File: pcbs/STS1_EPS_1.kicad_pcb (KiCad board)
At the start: 4 copper layers, 81 x 85 mm, 159 parts, among them J1 Inter-EPS, J2 Panel Y+, J4 Panel Y-, J5 Panel X+, J6 Panel X-, J7 Panel Z-, Q1 SI7135DP-T1-GE3, Q2 SI7135DP-T1-GE3, Q3 SI7135DP-T1-GE3, Q4 2N7002, Q5 2N7002, Q6 2N7002, Q7 2N7002, U1 LTC4020EUHFPBF, U10 MAX11632EEGT, U11 INA180A4, U12 BD50GA5WEFJ, U13 TPS259472ARPW, U14 LM334M, U15 LM334M, U16 LM334M, U17 LM334M, U18 LM334M, U19 TPS259472ARPW, U2 SI7272DP-T1-GE3, U20 TPS259472ARPW, U21 TPS259472ARPW, U22 TPS259472ARPW, U23 TPS259472ARPW, U24 TPS259472ARPW, U27 LTC4451AV#TRMPBF, U28 LTC4451AV#TRMPBF, U3 SI7272DP-T1-GE3, U4 TPS259472ARPW, U5 MAX11632EEGT, U6 MAX11632EEGT, U7 MAX11632EEGT, U8 MAX11632EEGT, U9 MAX11632EEGT

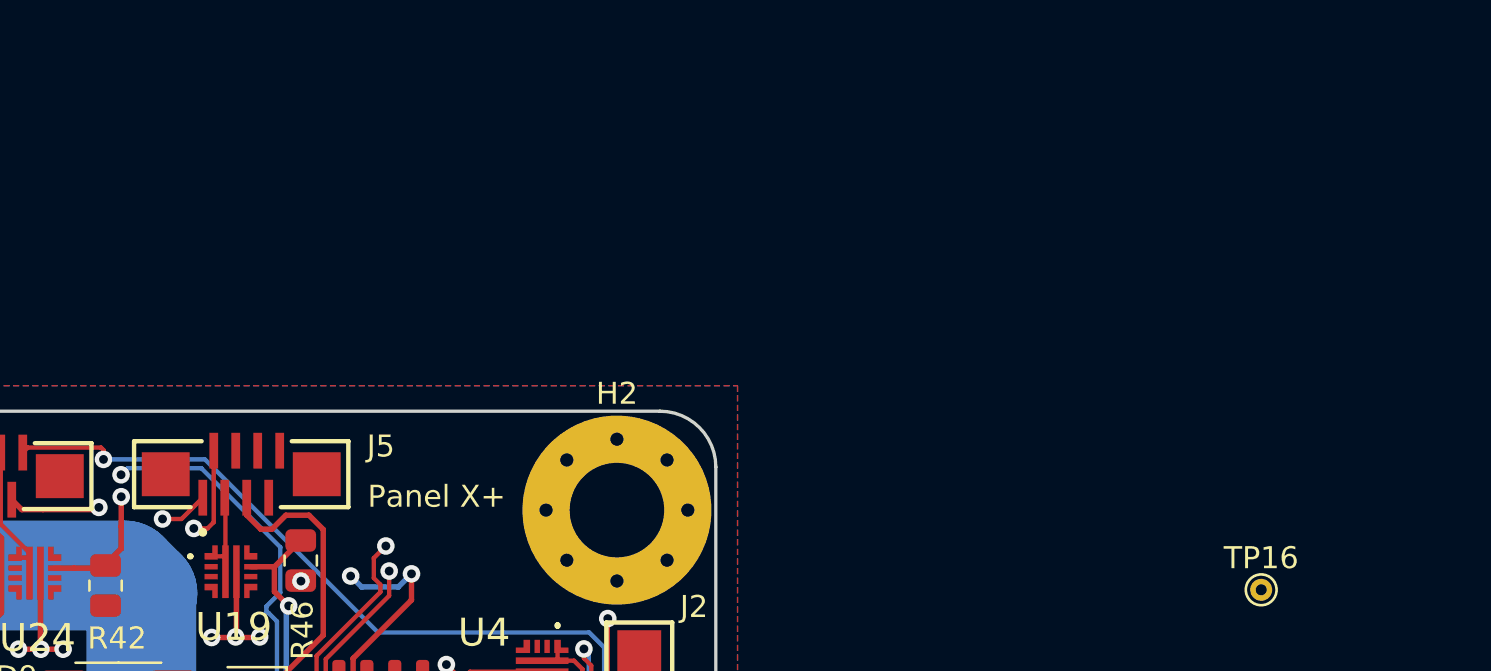
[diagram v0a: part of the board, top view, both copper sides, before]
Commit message: Removed UCI connector from STS1_EPS_2 and merged UCI connector with J5 on STS1_EPS_1.
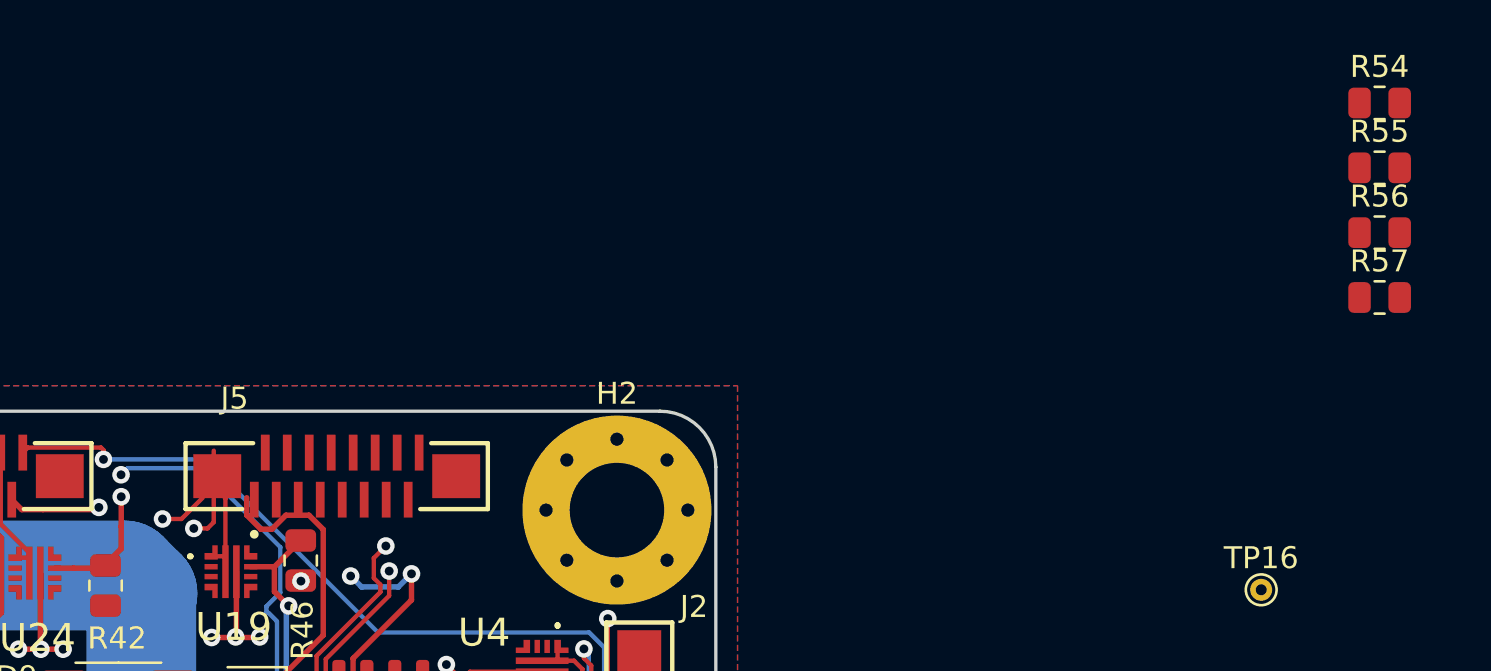
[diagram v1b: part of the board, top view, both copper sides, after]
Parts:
- added R54: 820, Resistor_SMD:R_0805_2012Metric, F.Cu at (176.9, 67.3)
- added R55: 332k, Resistor_SMD:R_0805_2012Metric, F.Cu at (176.9, 70.3)
- added R56: 332k, Resistor_SMD:R_0805_2012Metric, F.Cu at (176.9, 73.2)
- added R57: 390k, Resistor_SMD:R_0805_2012Metric, F.Cu at (176.9, 76.2)
- J5: footprint STS_Connector:SAMTEC_ZF5S-08-03-T-WT -> STS_Connector:SAMTEC_ZF5S-16-03-T-WT
- moved J5 4.34 mm to (129.4, 84.3)
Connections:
- net /Cubesat Bus Interface/UCI_COBC_UART_1 renamed /Cubesat Bus Interface/UCI_COBC_UART_TX
- net /Cubesat Bus Interface/UCI_COBC_UART_2 renamed /Cubesat Bus Interface/UCI_COBC_UART_RX
- CSBI_2 pad 13: /BAT_FAULT -> Net-(CSBI_2-Pin_13)
- CSBI_2 pad 14: /BAT_FAULT -> Net-(CSBI_2-Pin_13)
- CSBI_2 pad 17: GND -> Net-(CSBI_2-Pin_17)
- CSBI_2 pad 18: GND -> Net-(CSBI_2-Pin_17)
- CSBI_2 pad 19: Net-(CSBI_2-Pin_19) -> /BAT_FAULT
- CSBI_2 pad 20: Net-(CSBI_2-Pin_19) -> /BAT_FAULT
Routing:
- net Net-(CSBI_2-Pin_19): track 2.00 -> 0.00 mm
- net Net-(CSBI_2-Pin_17): track 0.00 -> 2.00 mm
- net GND: track 106.2 -> 104.2 mm
- net /BAT_FAULT: track 75.1 -> 77.1 mm

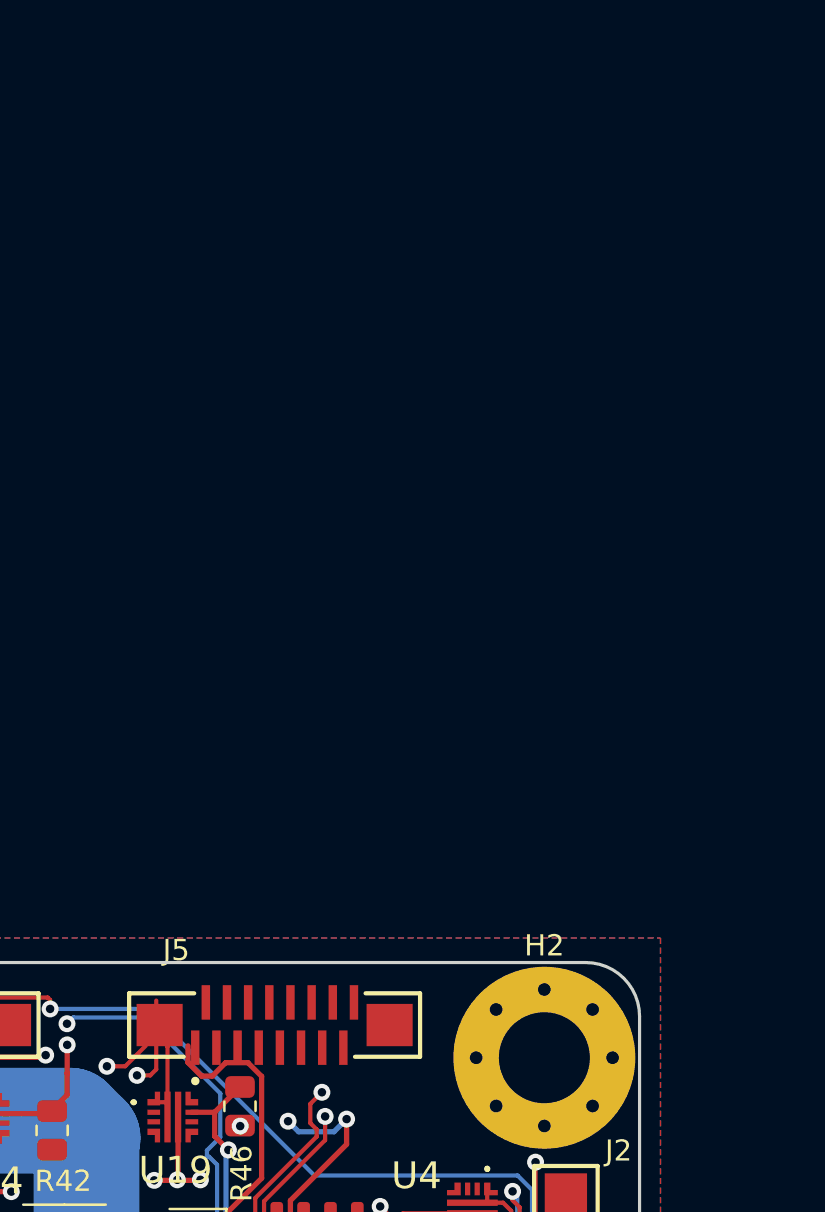
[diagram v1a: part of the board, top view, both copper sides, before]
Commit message: Added TVS diodes.
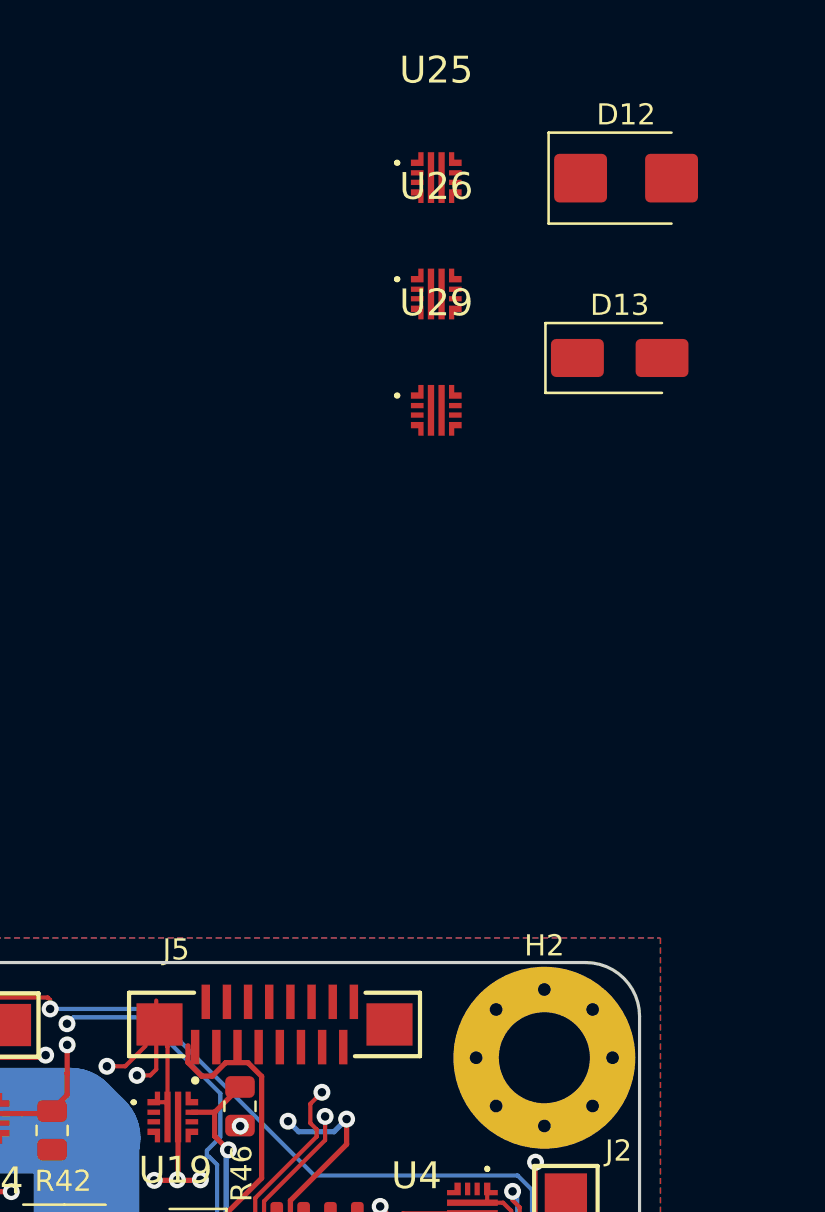
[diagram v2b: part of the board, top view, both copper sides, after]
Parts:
- added D12: SM6T6V8A, Diode_SMD:D_SMB, F.Cu at (146.1, 44.3)
- added D13: PTVS5V0Z1USK, Diode_SMD:D_SMA, F.Cu at (145.8, 52.8)
- added U25: TPS259472ARPW, STS_Package_DFN_QFN:TPS259472ARPWR, F.Cu at (137.1, 44.3)
- added U26: TPS259472ARPW, STS_Package_DFN_QFN:TPS259472ARPWR, F.Cu at (137.1, 49.8)
- added U29: TPS259472ARPW, STS_Package_DFN_QFN:TPS259472ARPWR, F.Cu at (137.1, 55.3)

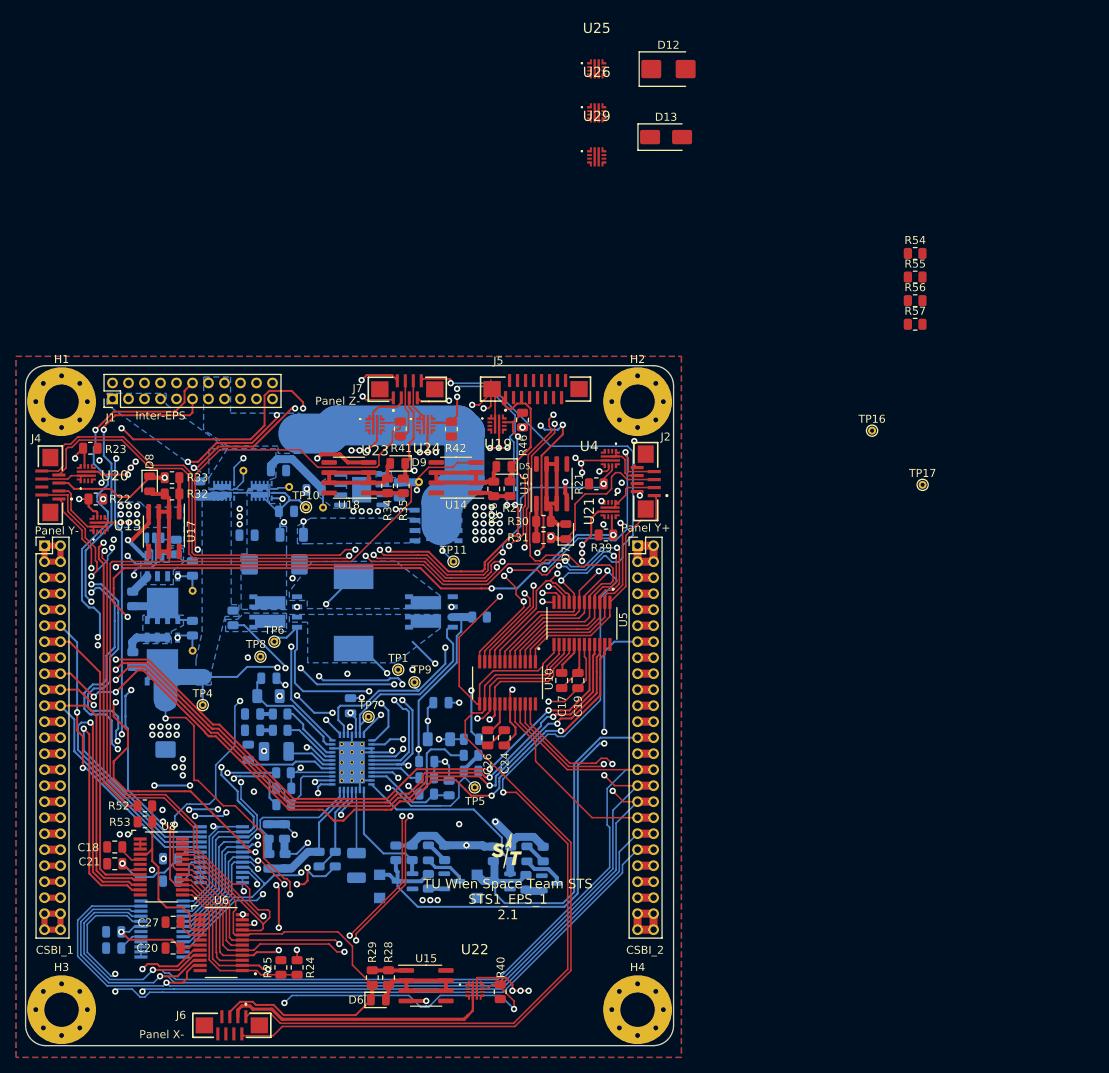
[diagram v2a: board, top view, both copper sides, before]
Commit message: Reoriented coordinate system.
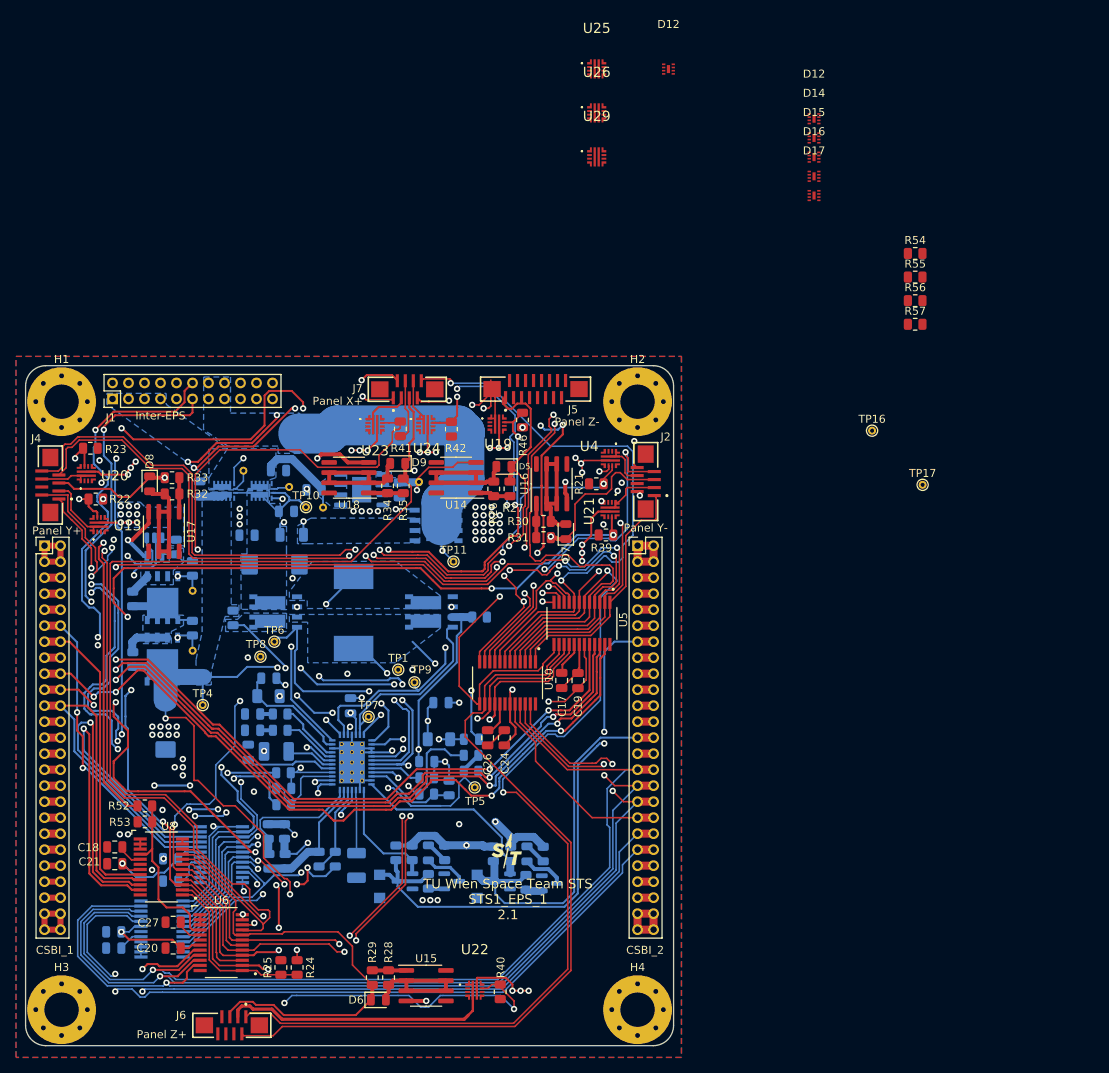
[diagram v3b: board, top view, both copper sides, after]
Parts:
- removed D13: PTVS5V0Z1USK, Diode_SMD:D_SMA
- added D12: ~, STS_Misc:LLP1713-9L, F.Cu at (164.2, 50.5)
- added D14: ~, STS_Misc:LLP1713-9L, F.Cu at (164.2, 52.9)
- added D15: ~, STS_Misc:LLP1713-9L, F.Cu at (164.2, 55.3)
- added D16: ~, STS_Misc:LLP1713-9L, F.Cu at (164.2, 57.7)
- added D17: ~, STS_Misc:LLP1713-9L, F.Cu at (164.2, 60.1)
- D12: value SM6T6V8A -> ~; footprint Diode_SMD:D_SMB -> STS_Misc:LLP1713-9L
- J2: value Panel Y+ -> Panel Y-
- J4: value Panel Y- -> Panel Y+
- J5: value Panel X+ -> Panel Z-
- J6: value Panel X- -> Panel Z+
- J7: value Panel Z- -> Panel X+
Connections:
- net Net-(CSBI_2-Pin_10) renamed /UCI_COBC_SWDIO
- net Net-(CSBI_2-Pin_13) renamed /UCI_COBC_SWO
- net Net-(CSBI_2-Pin_15) renamed /UCI_COBC_NOT_RST
- CSBI_2 pad 11: Net-(CSBI_2-Pin_11) -> /UCI_COBC_SWCLK
- CSBI_2 pad 12: Net-(CSBI_2-Pin_11) -> /UCI_COBC_SWCLK
- CSBI_2 pad 17: Net-(CSBI_2-Pin_17) -> /UCI_COBC_5V
- CSBI_2 pad 18: Net-(CSBI_2-Pin_17) -> /UCI_COBC_5V
- D12 pad 1: unconnected-(D12-A1-Pad1) -> /Panel_X-_1
- D12 pad 2: unconnected-(D12-A2-Pad2) -> /Panel_X-_2
- J5 pad 10: /Solar Cell Connectors/COBC_SWDCLK -> /UCI_COBC_SWCLK
- J5 pad 11: /Solar Cell Connectors/5V_ext -> /UCI_COBC_5V
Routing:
- net Net-(CSBI_2-Pin_17): track 2.00 -> 0.00 mm
- net Net-(CSBI_2-Pin_11): track 2.00 -> 0.00 mm
- net /UCI_COBC_SWCLK: track 0.00 -> 2.00 mm
- net /UCI_COBC_5V: track 0.00 -> 2.00 mm

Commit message: Intermediate commit.
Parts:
- removed C1: 50u, Capacitor_Tantalum_SMD:CP_EIA-3528-12_Kemet-T
- added C12: 50u, Capacitor_Tantalum_SMD:CP_EIA-3528-12_Kemet-T, B.Cu at (107.0, 143.8)
- added R58: 100k, Resistor_SMD:R_0805_2012Metric, F.Cu at (184.6, 42.8)
- added R59: 100k, Resistor_SMD:R_0805_2012Metric, F.Cu at (184.6, 45.7)
- added R60: 100k, Resistor_SMD:R_0805_2012Metric, F.Cu at (184.6, 48.6)
- added R61: 100k, Resistor_SMD:R_0805_2012Metric, F.Cu at (184.6, 51.6)
- added R62: 100k, Resistor_SMD:R_0805_2012Metric, F.Cu at (196.1, 64.5)
- added R63: 100k, Resistor_SMD:R_0805_2012Metric, F.Cu at (197.4, 62.0)
- R54, R55, R56, R57, U25, U26, U29: moved to B.Cu
- moved TP16 68.7 mm to (103.0, 84.8)
- moved R55 58.4 mm to (124.2, 95.5), turned to 90 degrees
- moved R54 51.7 mm to (130.8, 90.9), turned to -90 degrees
- moved U25 46.2 mm to (134.4, 90.4), turned to -90 degrees
- moved U26 46.0 mm to (127.6, 94.8), turned to 180 degrees
- moved R57 41.4 mm to (138.2, 91.0), turned to -90 degrees
- moved U29 40.2 mm to (163.0, 86.0), turned to 180 degrees
- moved R56 22.3 mm to (158.8, 86.2), turned to 90 degrees
- moved R46 1.12 mm to (127.5, 89.2)
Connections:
- CSBI_1 pad 43: /Cubesat Bus Interface/UART_COBC_EDU_2 -> unconnected-(CSBI_1-Pin_43-Pad43)
- CSBI_1 pad 44: /Cubesat Bus Interface/UART_COBC_EDU_2 -> unconnected-(CSBI_1-Pin_44-Pad44)
- CSBI_1 pad 45: /Cubesat Bus Interface/UART_COBC_EDU_1 -> unconnected-(CSBI_1-Pin_45-Pad45)
- CSBI_1 pad 46: /Cubesat Bus Interface/UART_COBC_EDU_1 -> unconnected-(CSBI_1-Pin_46-Pad46)
- J1 pad 17: /CENTER -> /BATT_RAW
- J1 pad 18: /BATT_RAW -> /CENTER
- J1 pad 21: /V_LOGIC -> GND
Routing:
- net /Cubesat Bus Interface/UCI_COBC_UART_TX: track 2.00 -> 26.1 mm
- net /Panel_Y+_7: track 47.5 -> 25.1 mm
- net /Panel_Z-_8: track 71.1 -> 57.2 mm
- net Net-(U25-OVCSEL): track 0.00 -> 11.0 mm
- net /Solar Cell Connectors/UCI_UART_TX_CONN: track 0.00 -> 9.96 mm, vias 0 -> 1
- net /Panel_X+_2: track 70.5 -> 80.2 mm
- net /MPPT_SUM: track 207.1 -> 215.7 mm
- net /Panel_Z-_7: track 80.8 -> 89.3 mm, vias 5 -> 2
- net /BAT_FAULT: track 77.1 -> 70.2 mm
- net /Panel_X+_1: track 63.4 -> 69.3 mm
- net /Panel_Z-_2: track 96.3 -> 102.0 mm
- net Net-(U25-ILM): track 0.00 -> 4.15 mm
- net (no net): track 0.00 -> 4.00 mm
- net GND: track 104.2 -> 107.8 mm
- net /Panel_X+_5: track 118.8 -> 115.5 mm
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- added copper zone on F.Cu, net (none)
- added copper zone on B.Cu, net /BATT_RAW
- added copper zone on In4.Cu, net /BATT_RAW
- added copper zone on B.Cu, net /Solar Cell Connectors/Bat+
- added copper zone on In3.Cu, net GND
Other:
- copper layers 4 -> 6
